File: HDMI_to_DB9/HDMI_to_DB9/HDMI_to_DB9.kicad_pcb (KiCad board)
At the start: 2 copper layers, 107 x 229.1 mm, 30 parts, among them J1 HDMI_A, J2 HDMI_A, J3 HDMI_A, J4 HDMI_A, J5 HDMI_A, J6 HDMI_A, J7 HDMI_A, J8 HDMI_A, J9 HDMI_A

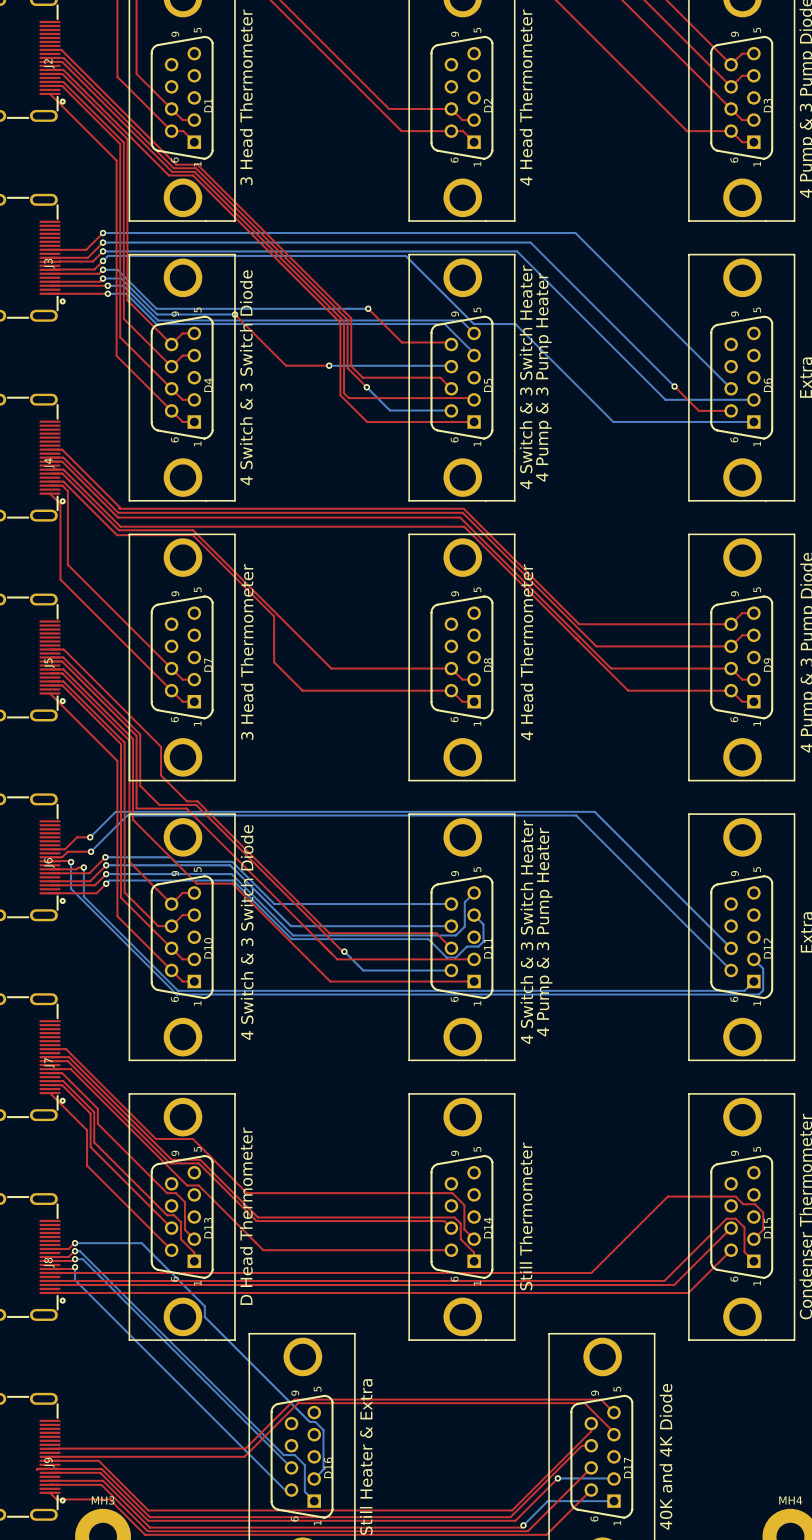
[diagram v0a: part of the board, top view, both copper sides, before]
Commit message: Updated Heater Traces
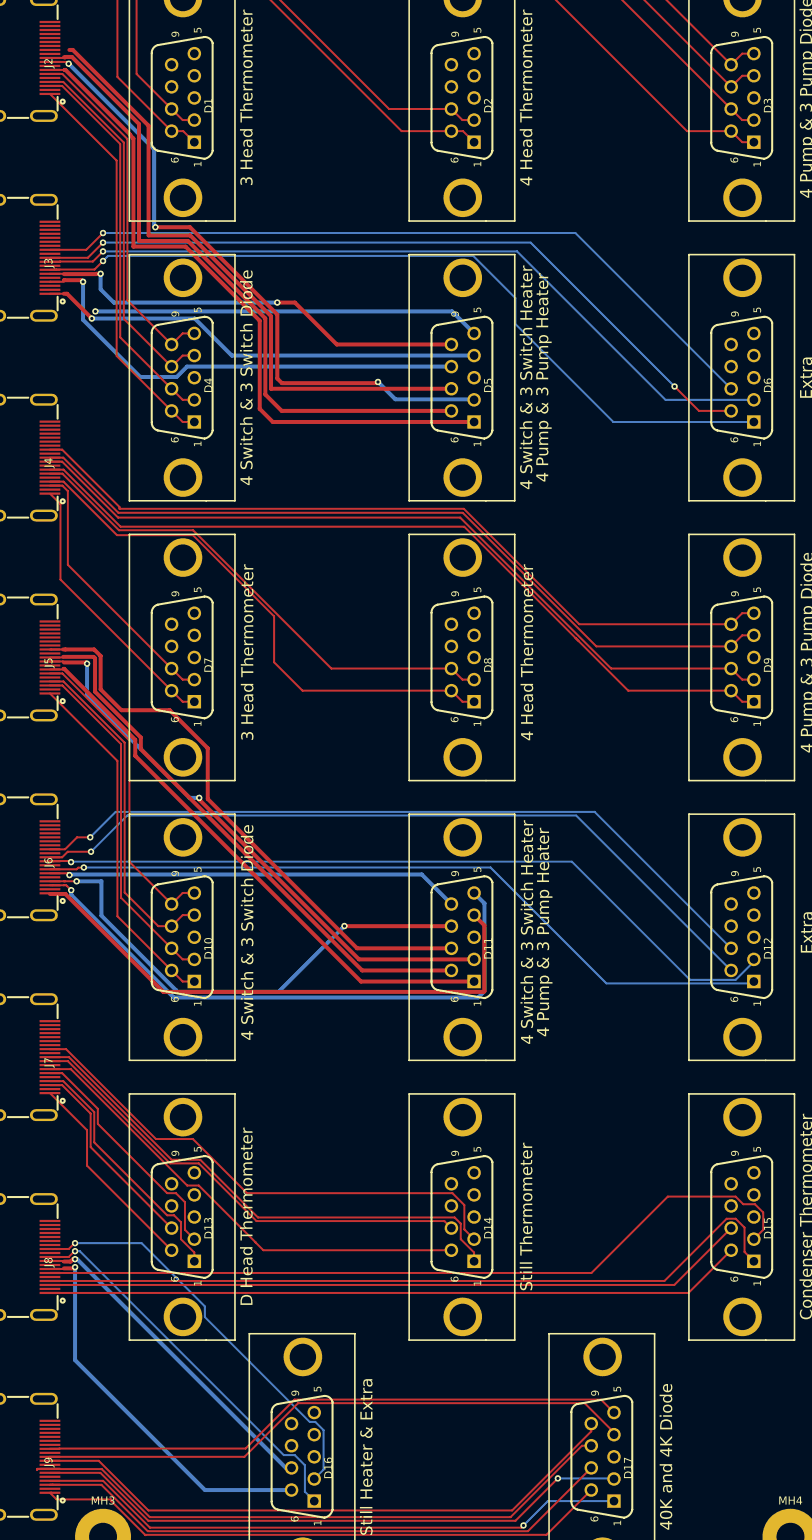
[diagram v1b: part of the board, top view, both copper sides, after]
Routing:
- net Net-(D11-Pad5): track 60.8 -> 73.7 mm
- net Net-(D5-Pad6): track 72.0 -> 83.5 mm, vias 1 -> 0
- net Net-(D5-Pad1): track 76.6 -> 85.8 mm
- net Net-(D11-Pad8): track 54.2 -> 62.1 mm, vias 1 -> 2
- net Net-(D5-Pad7): track 71.3 -> 78.7 mm
- net Net-(D12-Pad2): track 102.7 -> 95.5 mm
- net Net-(D5-Pad5): track 55.5 -> 48.6 mm
- net Net-(D16-Pad6): track 42.9 -> 49.8 mm
- net Net-(D11-Pad4): track 63.5 -> 69.5 mm, vias 1 -> 0
- net Net-(D5-Pad2): track 75.8 -> 81.3 mm, vias 0 -> 3
- net Net-(D11-Pad1): track 75.1 -> 70.4 mm
- net Net-(D11-Pad2): track 75.6 -> 71.1 mm, vias 0 -> 2
- net Net-(D11-Pad7): track 67.8 -> 72.2 mm
- net Net-(D5-Pad8): track 54.9 -> 58.8 mm, vias 3 -> 1
- net Net-(D12-Pad1): track 97.2 -> 94.3 mm
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
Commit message: Fixed
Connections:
- J1 pad 17: GND -> Net-(J1-Pad17)
- J1 pad 20: (no net) -> GND
- J1 pad 21: (no net) -> GND
- J1 pad 22: (no net) -> GND
- J1 pad 23: (no net) -> GND
- J2 pad 17: GND -> Net-(J2-Pad17)
- J2 pad 20: (no net) -> GND
- J2 pad 21: (no net) -> GND
- J2 pad 22: (no net) -> GND
- J2 pad 23: (no net) -> GND
- J3 pad 17: GND -> Net-(J3-Pad17)
- J3 pad 20: (no net) -> GND
- J3 pad 21: (no net) -> GND
- J3 pad 22: (no net) -> GND
- J3 pad 23: (no net) -> GND
- J4 pad 17: GND -> Net-(J4-Pad17)
- J4 pad 20: (no net) -> GND
- J4 pad 21: (no net) -> GND
- J4 pad 22: (no net) -> GND
- J4 pad 23: (no net) -> GND
- J5 pad 17: GND -> Net-(J5-Pad17)
- J5 pad 20: (no net) -> GND
- J5 pad 21: (no net) -> GND
- J5 pad 22: (no net) -> GND
- J5 pad 23: (no net) -> GND
- J6 pad 17: GND -> Net-(J6-Pad17)
- J6 pad 20: (no net) -> GND
- J6 pad 21: (no net) -> GND
- J6 pad 22: (no net) -> GND
- J6 pad 23: (no net) -> GND
- J7 pad 17: GND -> Net-(J7-Pad17)
- J7 pad 20: (no net) -> GND
- J7 pad 21: (no net) -> GND
- J7 pad 22: (no net) -> GND
- J7 pad 23: (no net) -> GND
- J8 pad 10: Net-(D16-Pad1) -> Net-(D16-Pad6)
- J8 pad 12: Net-(D16-Pad2) -> Net-(D16-Pad7)
- J8 pad 17: GND -> Net-(J8-Pad17)
- J8 pad 20: (no net) -> GND
- J8 pad 21: (no net) -> GND
- J8 pad 22: (no net) -> GND
- J8 pad 23: (no net) -> GND
- J8 pad 7: Net-(D16-Pad6) -> Net-(D16-Pad1)
- J8 pad 9: Net-(D16-Pad7) -> Net-(D16-Pad2)
- J9 pad 1: Net-(D17-Pad6) -> Net-(D17-Pad1)
- J9 pad 10: Net-(D17-Pad4) -> Net-(D17-Pad8)
- J9 pad 12: Net-(D17-Pad5) -> Net-(D17-Pad9)
- J9 pad 17: GND -> Net-(J9-Pad17)
- J9 pad 20: (no net) -> GND
- J9 pad 21: (no net) -> GND
- J9 pad 22: (no net) -> GND
- J9 pad 23: (no net) -> GND
- J9 pad 3: Net-(D17-Pad7) -> Net-(D17-Pad2)
- J9 pad 4: Net-(D17-Pad1) -> Net-(D17-Pad6)
- J9 pad 6: Net-(D17-Pad2) -> Net-(D17-Pad7)
- J9 pad 7: Net-(D17-Pad8) -> Net-(D17-Pad4)
- J9 pad 9: Net-(D17-Pad9) -> Net-(D17-Pad5)
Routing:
- net Net-(D5-Pad5): track 48.6 -> 56.2 mm
- net Net-(D16-Pad1): track 48.3 -> 55.5 mm
- net Net-(D16-Pad2): track 51.6 -> 56.7 mm
- net Net-(D17-Pad8): track 77.2 -> 74.2 mm
- net Net-(D5-Pad7): track 78.7 -> 81.0 mm
- net Net-(D16-Pad7): track 41.5 -> 43.4 mm, vias 1 -> 2
- net Net-(D17-Pad5): track 73.8 -> 75.6 mm, vias 0 -> 2
- net Net-(D17-Pad9): track 75.4 -> 77.2 mm
- net Net-(D16-Pad6): track 49.8 -> 48.4 mm, vias 1 -> 2
- net Net-(D17-Pad4): track 75.1 -> 76.4 mm, vias 0 -> 2
- net Net-(D17-Pad7): track 73.8 -> 74.4 mm
- net Net-(D17-Pad2): track 75.3 -> 75.0 mm, vias 1 -> 3
- net Net-(D17-Pad1): track 74.4 -> 74.3 mm, vias 1 -> 2
